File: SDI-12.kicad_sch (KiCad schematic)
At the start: 42 parts, among them J1 USB_B_Micro, J2 Conn_SWD, J3 SDI-12_OUT, J4 SDI12_POWER, Q1 BSS138, Q2 BSS138, Q3 BSS138, SW1 SW_Push, SW2 RESET_SW, U1 LDI1117-3.3H, U2 STM32F103C8Tx, U3 74LVC1G125GW,125, Y1 24MHz 15pF

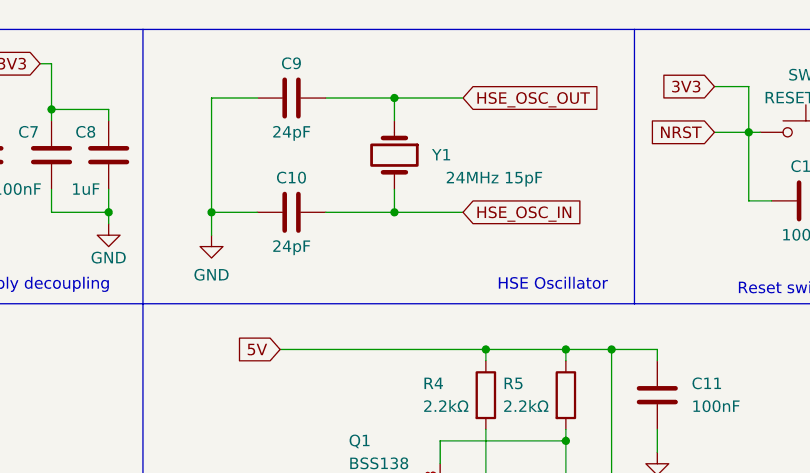
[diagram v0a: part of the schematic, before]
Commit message: - Crystal oscillator value changed to proper 16MHz - Minor font changes - Readme document - git lfs for readme graphics
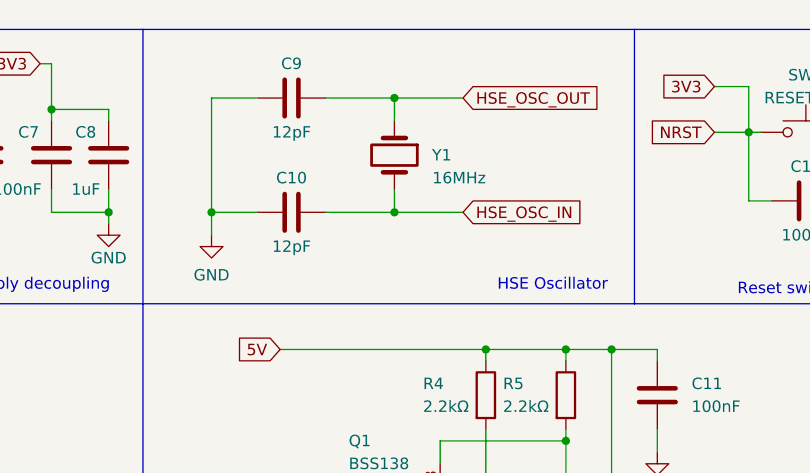
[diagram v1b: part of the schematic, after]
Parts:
- C10, C9: value 24pF -> 12pF
- Y1: value 24MHz 15pF -> 16MHz
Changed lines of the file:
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@@
       (effects (font (size 1.27 1.27)))
     )
-    (property "Value" "24pF" (at 151.13 25.4 90)
+    (property "Value" "12pF" (at 151.13 25.4 90)
       (effects (font (size 1.27 1.27)))
     )
@@
       (effects (font (size 1.27 1.27)) (justify right))
     )
-    (property "Value" "24MHz 15pF" (at 179.07 30.48 90)
+    (property "Value" "16MHz" (at 172.72 30.48 90)
       (effects (font (size 1.27 1.27)) (justify right))
     )
@@
       (effects (font (size 1.27 1.27)))
     )
-    (property "Value" "24pF" (at 151.13 38.1 90)
-      (effects (font (size 1.27 1.27)))
-    )
+    (property "Value" "12pF" (at 151.13 38.1 90)
+      (effects (font (size 1.27 1.27)))
+    )

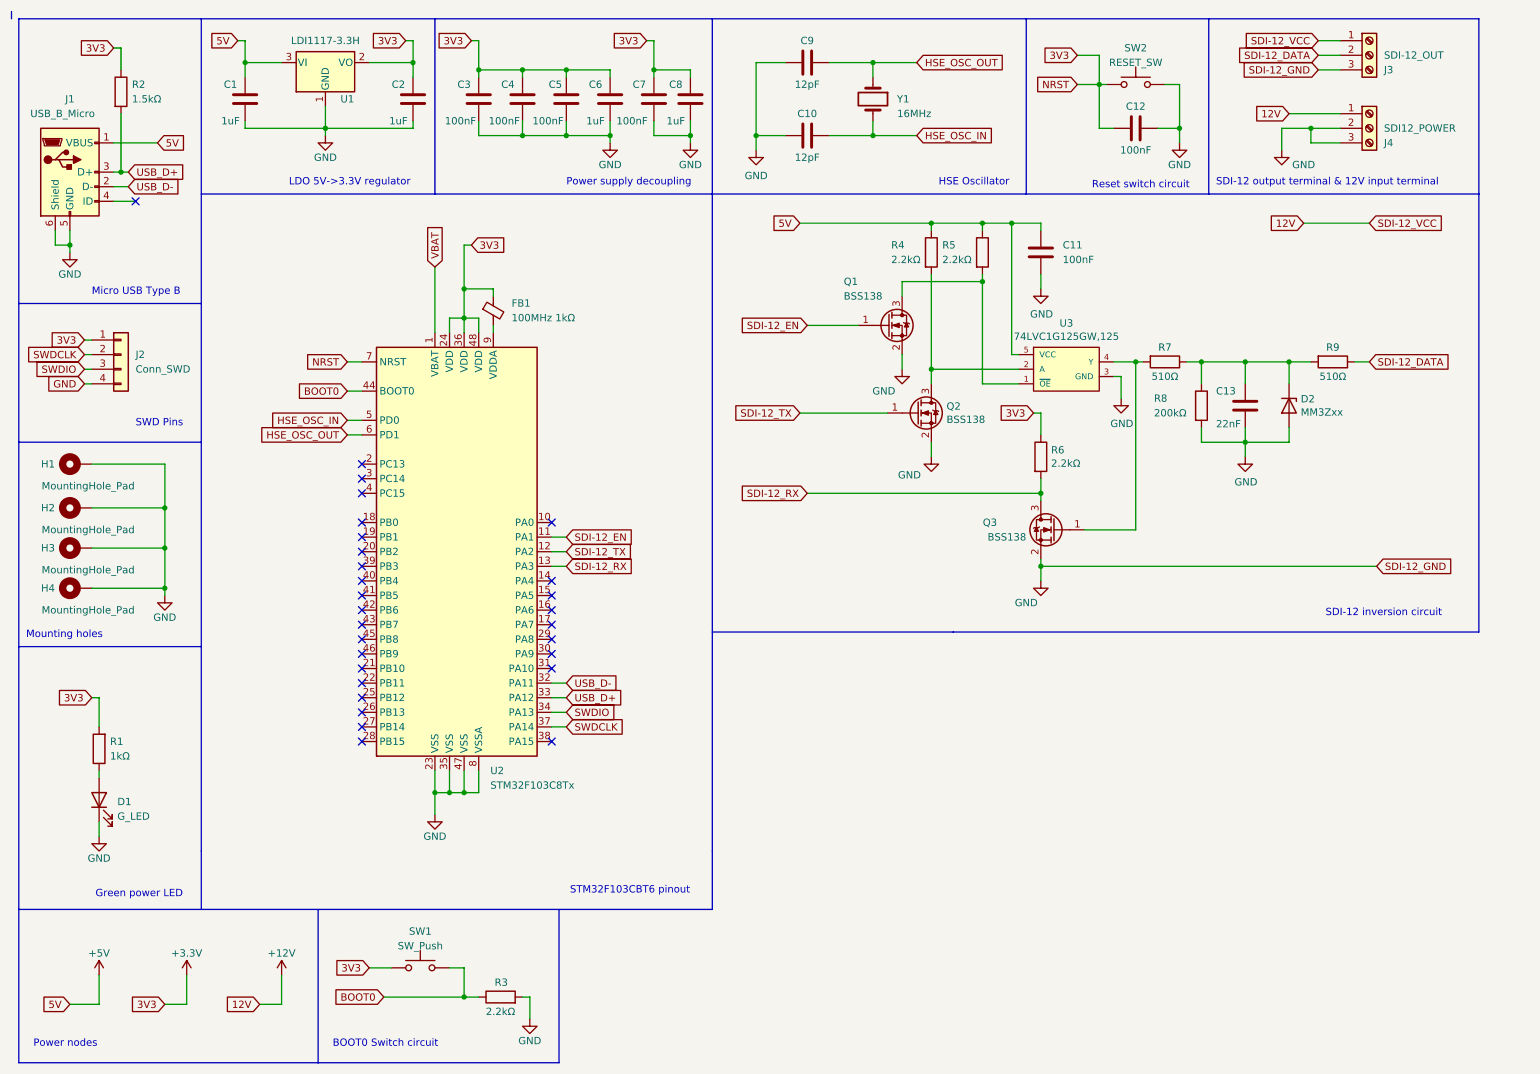
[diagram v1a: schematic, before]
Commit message: - STM32F103 replaced with G431 counterpart - TXS0102x for voltage level shifting - Added LED's for I/O status
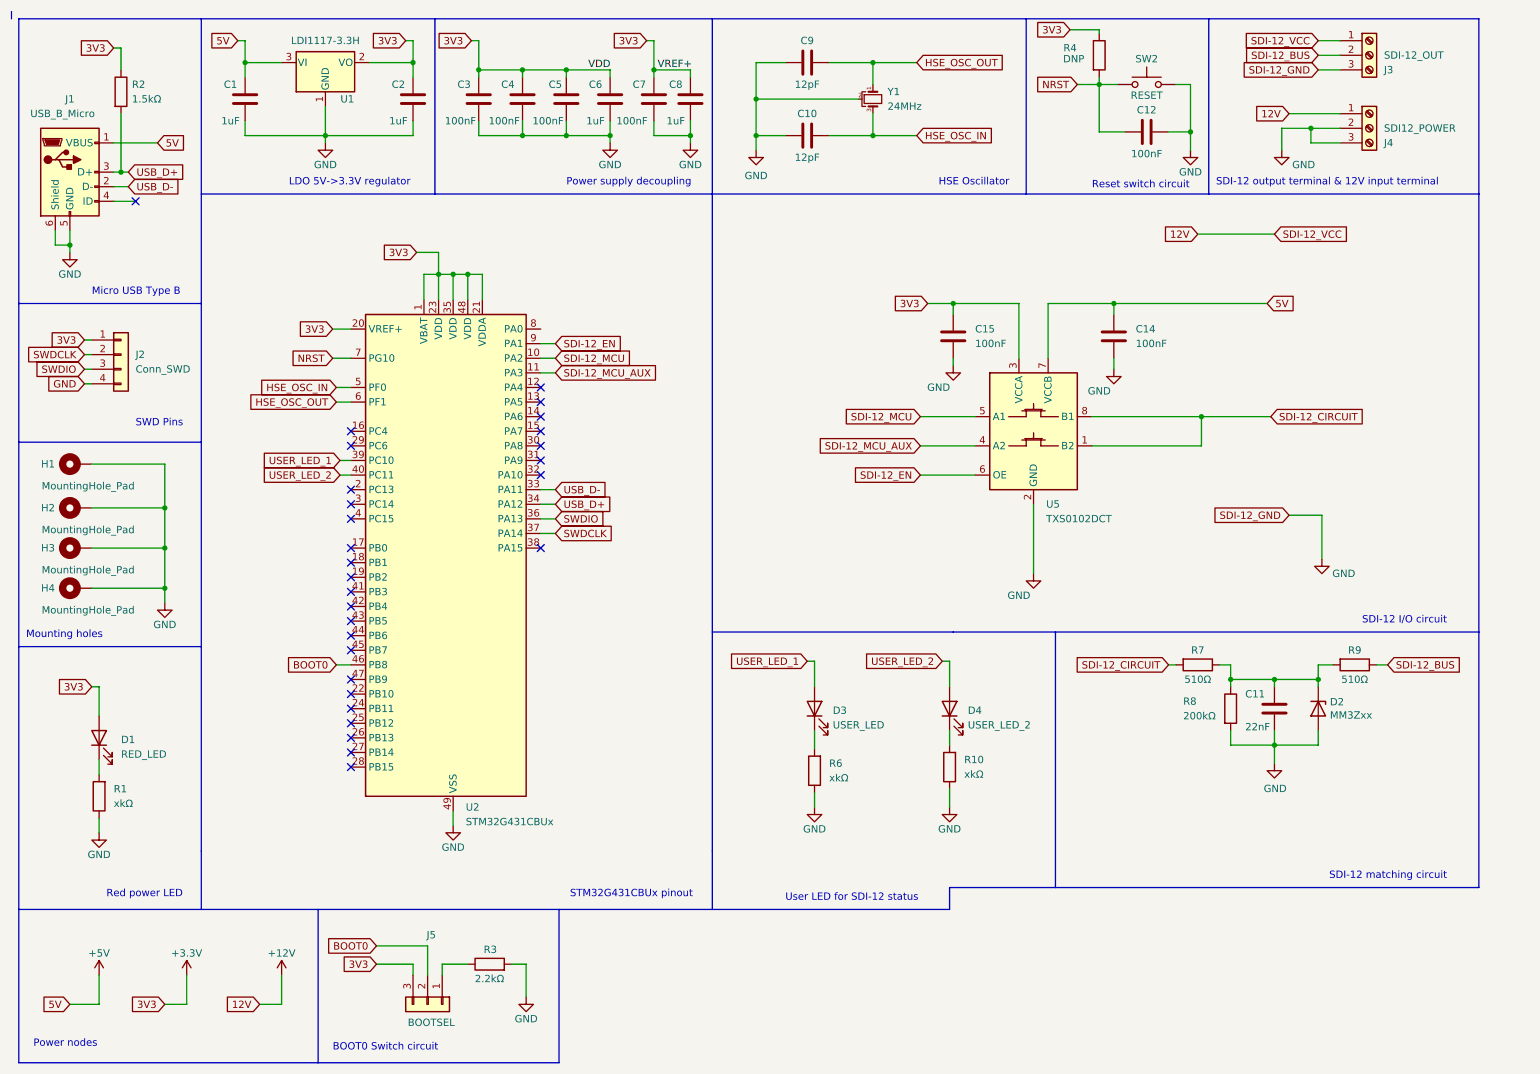
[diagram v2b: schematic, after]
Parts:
- removed C13: 22nF, Capacitor_SMD:C_0805_2012Metric, symbol Device:C
- removed FB1: 100MHz 1kΩ, Inductor_SMD:L_0805_2012Metric, symbol Device:FerriteBead_Small
- removed Q1, Q2, Q3: BSS138, Package_TO_SOT_SMD:SOT-23, symbol Transistor_FET:BSS138
- removed R5: 2.2kΩ, Resistor_SMD:R_0805_2012Metric, symbol Device:R
- removed SW1: SW_Push, Button_Switch_SMD:SW_SPST_B3U-1000P, symbol Switch:SW_Push
- removed U2: STM32F103C8Tx, Package_QFP:LQFP-48_7x7mm_P0.5mm, symbol MCU_ST_STM32F1:STM32F103C8Tx
- removed U3: 74LVC1G125GW,125, Package_TO_SOT_SMD:SOT-353_SC-70-5, symbol SDI-12-rescue:74LVC1G125GW,125-eec-SDI-12-rescue
- removed Y1: 16MHz, Crystal:Crystal_SMD_2016-4Pin_2.0x1.6mm, symbol Device:Crystal
- added C14, C15: 100nF, Capacitor_SMD:C_0603_1608Metric, symbol Device:C
- added D3: USER_LED, LED_SMD:LED_0805_2012Metric, symbol Device:LED
- added D4: USER_LED_2, LED_SMD:LED_0805_2012Metric, symbol Device:LED
- added J5: BOOTSEL, Connector_PinHeader_2.54mm:PinHeader_1x03_P2.54mm_Vertical, symbol Connector_Generic:Conn_01x03
- added R10: xkΩ, Resistor_SMD:R_0603_1608Metric, symbol Device:R
- added U2: STM32G431CBUx, Package_DFN_QFN:QFN-48-1EP_7x7mm_P0.5mm_EP5.6x5.6mm, symbol MCU_ST_STM32G4:STM32G431CBUx
- added U5: TXS0102DCT, Package_SO:SSOP-8_2.95x2.8mm_P0.65mm, symbol Logic_LevelTranslator:TXS0102DCT
- added Y1: 24MHz, Crystal:Crystal_SMD_3225-4Pin_3.2x2.5mm, symbol Device:Crystal_GND2_Small
- C10, C12, C3, C4, C5, C7, C9: footprint Capacitor_SMD:C_0805_2012Metric -> Capacitor_SMD:C_0603_1608Metric
- C11: value 100nF -> 22nF; footprint Capacitor_SMD:C_0805_2012Metric -> Capacitor_SMD:C_0603_1608Metric
- D1: value G_LED -> RED_LED
- R1: value 1kΩ -> xkΩ; footprint Resistor_SMD:R_0805_2012Metric -> Resistor_SMD:R_0603_1608Metric
- R2, R3, R7, R8, R9: footprint Resistor_SMD:R_0805_2012Metric -> Resistor_SMD:R_0603_1608Metric
- R4: value 2.2kΩ -> DNP; footprint Resistor_SMD:R_0805_2012Metric -> Resistor_SMD:R_0603_1608Metric
- R6: value 2.2kΩ -> xkΩ; footprint Resistor_SMD:R_0805_2012Metric -> Resistor_SMD:R_0603_1608Metric
- SW2: value RESET_SW -> RESET
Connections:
- net +3.3V: now also D1.2 (A), R4.1, C15.1, J5.3 (Pin_3), U2.1 (VBAT), U2.20 (VREF+), U2.21 (VDDA), U2.23 (VDD), U2.35 (VDD), U2.48 (VDD), U5.3 (VCCA); no longer C12.1, R1.2, R6.1, SW2.1
- net +5V: now also C14.1, U5.7 (VCCB); no longer C11.1, R4.1
- net BOOT0: now also J5.2 (Pin_2), U2.46 (PB8); no longer R3.1
- net GND: now also R1.1, R6.1, C14.2, C15.2, R10.1, U2.49 (VSS), U5.2 (GND), Y1.2; no longer D1.1 (K)
- net HSE_OSC_IN: now also U2.5 (PF0), Y1.3
- net HSE_OSC_OUT: now also U2.6 (PF1), Y1.1
- net SDI-12_EN: now also U2.9 (PA1), U5.6 (OE)
- net SWDCLK: now also U2.37 (PA14)
- net SWDIO: now also U2.36 (PA13)
- net USB_D+: now also U2.34 (PA12)
- net USB_D-: now also U2.33 (PA11)
- net NRST: now reaches R4.2
- net NRST: now also C12.1, SW2.1, U2.7 (PG10)
- net SDI-12_CIRCUIT: now reaches R7.2
- net SDI-12_CIRCUIT: now also U5.1 (B2), U5.8 (B1)
- net at D2.1 (K), R7.1, R8.1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: now also C11.1
- net SDI-12_DATA renamed SDI-12_BUS
- net SDI-12_RX: no longer names the net of R6.2
- net SDI-12_RX: now also D3.1 (K)
- new net: D4.1 (K), R10.2
- new net: D1.1 (K), R1.2
- new net: J5.1 (Pin_1), R3.1
- new net SDI-12_MCU: U2.10 (PA2), U5.5 (A1)
- new net SDI-12_MCU_AUX: U2.11 (PA3), U5.4 (A2)
- new net USER_LED_1: D3.2 (A), U2.39 (PC10)
- new net USER_LED_2: D4.2 (A), U2.40 (PC11)
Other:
- note added: "Red power LED"
- note added: "SDI-12 I/O circuit"
- note added: "SDI-12 matching circuit"
- note added: "STM32G431CBUx pinout"
- note added: "User LED for SDI-12 status"
- note removed: "Green power LED"
- note removed: "SDI-12 inversion circuit"
- note removed: "STM32F103CBT6 pinout"
- moved on the sheet: C12, D1, R3, SW2
